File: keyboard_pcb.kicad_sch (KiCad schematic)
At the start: 215 parts, among them J1 USB, J2 , J3 Power, J4 I2C, SW1 SW_Push, SW10 SW_Push, SW100 SW_Push, SW101 SW_Push, SW102 SW_Push, SW103 SW_Push, SW104 SW_Push, SW105 SW_Push, SW11 SW_Push, SW12 SW_Push, SW13 SW_Push, SW14 SW_Push, SW15 SW_Push, SW16 SW_Push, SW17 SW_Push, SW18 SW_Push, SW19 SW_Push, SW2 SW_Push, SW20 SW_Push, SW21 SW_Push, SW22 SW_Push, SW23 SW_Push, SW24 SW_Push, SW25 SW_Push, SW26 SW_Push, SW27 SW_Push, SW28 SW_Push, SW29 SW_Push, SW3 SW_Push, SW30 SW_Push, SW31 SW_Push, SW32 SW_Push, SW33 SW_Push, SW34 SW_Push, SW35 SW_Push, SW36 SW_Push, SW37 SW_Push, SW38 SW_Push, SW39 SW_Push, SW4 SW_Push, SW40 SW_Push, SW41 SW_Push, SW42 SW_Push, SW43 SW_Push, SW44 SW_Push, SW45 SW_Push, SW46 SW_Push, SW47 SW_Push, SW48 SW_Push, SW49 SW_Push, SW5 SW_Push, SW50 SW_Push, SW51 SW_Push, SW52 SW_Push, SW53 SW_Push, SW54 SW_Push, SW55 SW_Push, SW56 SW_Push, SW57 SW_Push, SW58 SW_Push, SW59 SW_Push, SW6 SW_Push, SW60 SW_Push, SW61 SW_Push, SW62 SW_Push, SW63 SW_Push, SW64 SW_Push, SW65 SW_Push, SW66 SW_Push, SW67 SW_Push, SW68 SW_Push, SW69 SW_Push, SW7 SW_Push, SW70 SW_Push, SW71 SW_Push, SW72 SW_Push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

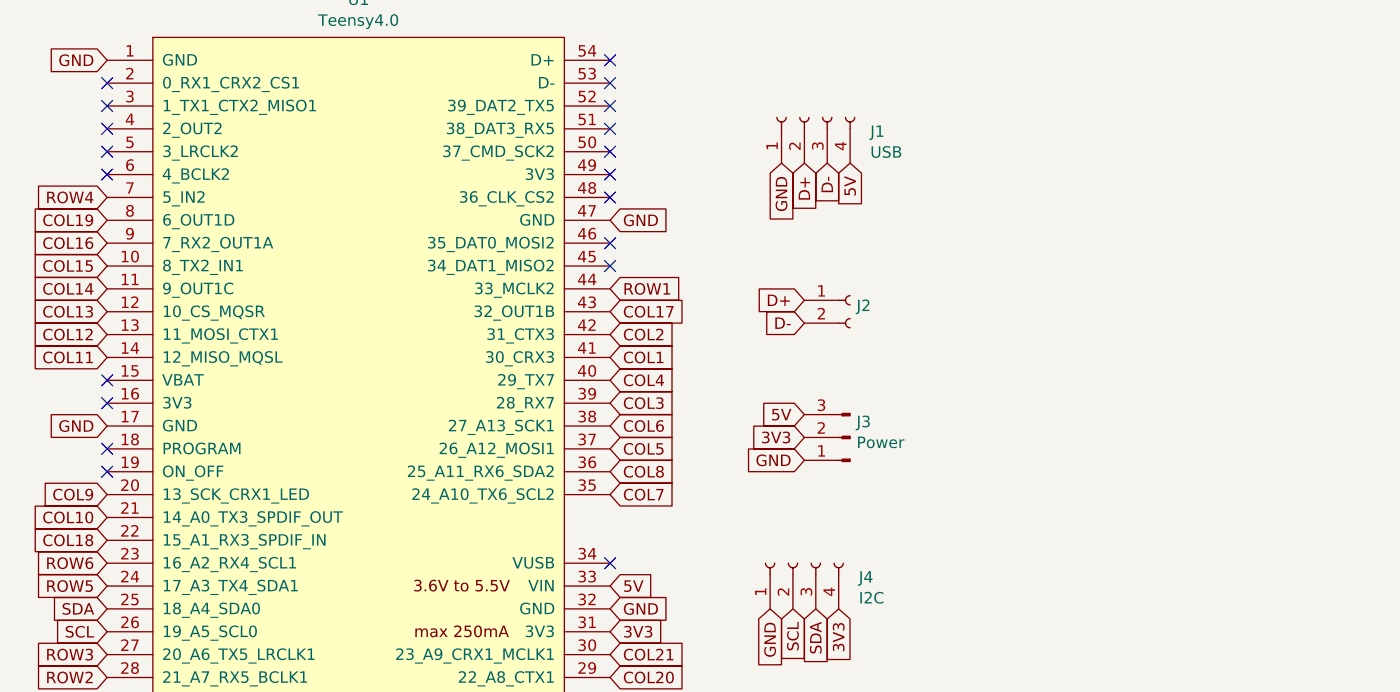
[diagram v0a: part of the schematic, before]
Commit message: Adjusted USB data line, added holes, some decoration
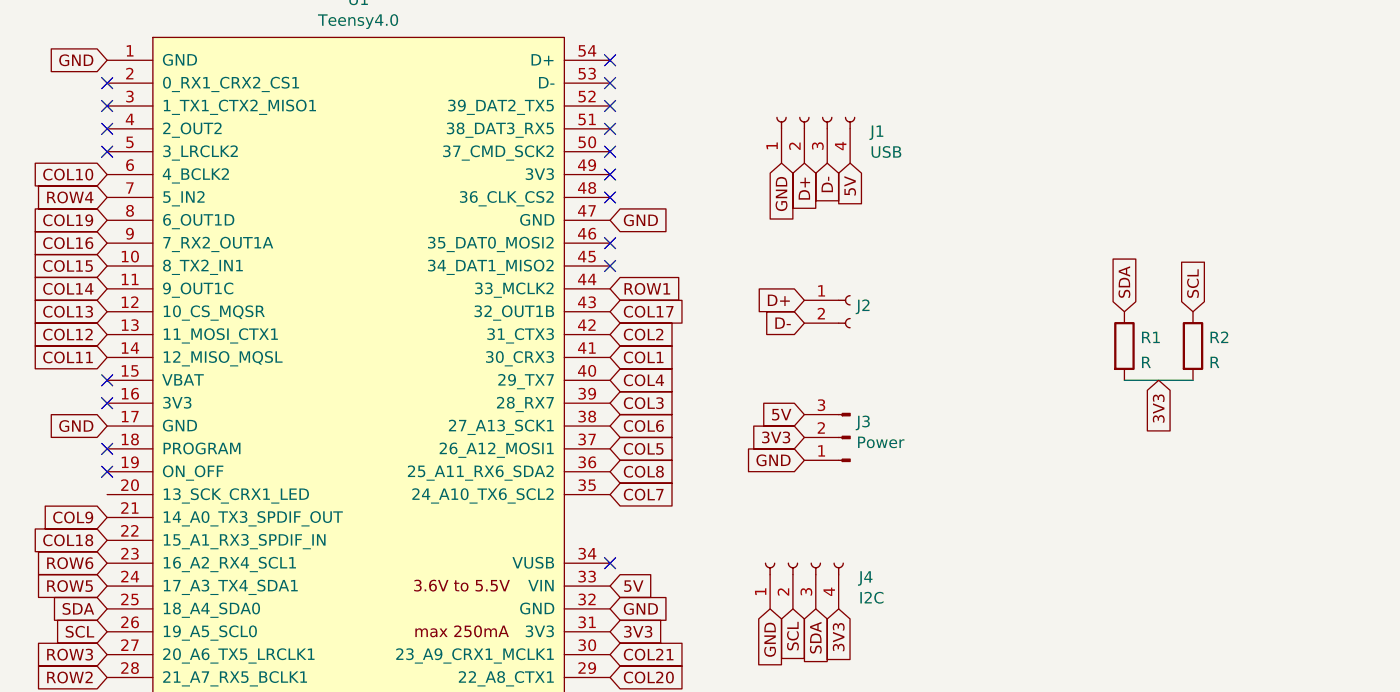
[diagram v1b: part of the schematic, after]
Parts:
- added R1, R2: R, Resistor_THT:R_Axial_DIN0207_L6.3mm_D2.5mm_P10.16mm_Horizontal, symbol Device:R
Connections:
- net 3V3: now also R1.2, R2.2
- net COL10: now also U1.6 (4_BCLK2); no longer U1.21 (14_A0_TX3_SPDIF_OUT)
- net COL9: now also U1.21 (14_A0_TX3_SPDIF_OUT); no longer U1.20 (13_SCK_CRX1_LED)
- net SCL: now also R2.1
- net SDA: now also R1.1
- no-connect marks 19 -> 18
